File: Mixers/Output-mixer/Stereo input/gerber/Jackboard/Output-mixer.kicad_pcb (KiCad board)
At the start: 2 copper layers, 135 x 110 mm, 131 parts, among them J1 In, J10 In, J11 In, J12 In, J14 Conn_01x04_Female, J17 Conn_01x02_Female, J2 In, J21 Jack 3.5 Out, J22 OutL, J23 OutR, J25 Conn_01x02_Female, J3 In, J4 In, J5 In, J6 In, J7 In, J8 In, J9 In, Q10 2N3904, Q5 2N3904, Q6 2N3904, Q7 2N3904, Q8 2N3904, Q9 2N3904, SW1 Mute, SW2 Mute, SW3 Mute, SW4 Mute, SW5 Mute, SW6 Mute, U1 TL072, U2 TL072, U3 TL072

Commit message: update gerbers for stereo mixer
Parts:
- removed C1, C2, C3, C4, C5, C6: .1µF, Capacitor_THT:CP_Radial_D5.0mm_P2.00mm
- removed C11, C14, C15, C16, C17, C18: 100nF, Capacitor_THT:C_Disc_D7.0mm_W2.5mm_P5.00mm
- removed the D1 at (76.4, 86.5)
- removed the D2 at (76.4, 105.0)
- removed the D3 at (76.4, 142.0)
- removed the D4 at (76.4, 49.5)
- removed the D5 at (76.4, 68.0)
- removed the D6 at (76.4, 123.5)
- removed Gain1, Gain2, Gain3, Gain4, Gain5, Gain6: 500k, Synth:Pot-bourns-alpha
- removed R1, R2, R3, R4, R5, R6: 2.2k, Resistor_THT:R_Axial_DIN0207_L6.3mm_D2.5mm_P10.16mm_Horizontal
- removed R10, R11, R12, R7, R8, R9: 100k, Resistor_THT:R_Axial_DIN0207_L6.3mm_D2.5mm_P10.16mm_Horizontal
- removed the R13 at (106.5, 41.8)
- removed the R14 at (107.0, 65.8)
- removed the R15 at (106.9, 76.0)
- removed the R16 at (107.3, 103.3)
- removed the R17 at (107.3, 113.0)
- removed the R18 at (107.5, 134.8)
- removed U1, U2, U3: TL072, Package_DIP:DIP-8_W7.62mm_Socket
- added J27: Conn_01x06_Female, Connector_PinSocket_2.54mm:PinSocket_1x06_P2.54mm_Vertical, B.Cu at (52.8, 45.8)
- added J28: Conn_01x06_Female, Connector_PinSocket_2.54mm:PinSocket_1x06_P2.54mm_Vertical, B.Cu at (52.8, 64.2)
- added J29: Conn_01x06_Female, Connector_PinSocket_2.54mm:PinSocket_1x06_P2.54mm_Vertical, B.Cu at (52.8, 82.8)
- added J30: Conn_01x06_Female, Connector_PinSocket_2.54mm:PinSocket_1x06_P2.54mm_Vertical, B.Cu at (52.8, 101.2)
- added J35: Conn_01x06_Female, Connector_PinSocket_2.54mm:PinSocket_1x06_P2.54mm_Vertical, B.Cu at (52.8, 119.8)
- added J36: Conn_01x06_Female, Connector_PinSocket_2.54mm:PinSocket_1x06_P2.54mm_Vertical, B.Cu at (52.8, 138.2)
- added J40: Conn_01x04_Female, Connector_PinSocket_2.54mm:PinSocket_1x04_P2.54mm_Vertical, B.Cu at (82.2, 81.8)
- added RV1: 50k, Synth:PTV1124420AA503, F.Cu at (72.8, 42.5)
- added RV2: 50k, Synth:PTV1124420AA503, F.Cu at (72.8, 61.0)
- added RV3: 50k, Synth:PTV1124420AA503, F.Cu at (72.8, 79.5)
- added RV4: 50k, Synth:PTV1124420AA503, F.Cu at (72.8, 98.0)
- added RV5: 50k, Synth:PTV1124420AA503, F.Cu at (72.8, 116.5)
- added RV6: 50k, Synth:PTV1124420AA503, F.Cu at (72.8, 135.0)
- moved J10 41.6 mm to (22.0, 107.0)
- moved J12 41.6 mm to (22.0, 125.5)
- moved J6 41.6 mm to (22.0, 70.0)
- moved R21 40.7 mm to (82.0, 139.1), turned to 90 degrees
- moved R14 35.0 mm to (85.5, 54.2), turned to -90 degrees
- moved R22 33.5 mm to (85.5, 128.9), turned to -90 degrees
- moved R20 33.2 mm to (85.5, 110.6), turned to -90 degrees
- moved R18 32.6 mm to (86.1, 97.5)
- moved R15 32.4 mm to (76.0, 73.0)
- moved R24 32.3 mm to (85.5, 36.5), turned to -90 degrees
- moved Pan1 31.8 mm to (97.0, 65.5)
- moved Pan2 31.8 mm to (97.0, 84.0)
- moved Pan3 31.8 mm to (97.0, 102.5)
- moved Pan4 31.8 mm to (97.0, 121.0)
- moved Pan5 31.8 mm to (97.0, 139.6)
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- renumbered D7 to D1, D8 to D2, D9 to D3, D10 to D4, D11 to D5, D12 to D6, Pan2 to Pan1, Pan3 to Pan2, Pan4 to Pan3, Pan5 to Pan4, Pan6 to Pan5, Pan1 to Pan6, R21 to R13, R22 to R14, R23 to R15, R24 to R16, R25 to R17, R26 to R18, R27 to R19, R28 to R20, R29 to R21, R30 to R22, R19 to R23, R20 to R24, R31 to R25, R32 to R26, R33 to R27, R34 to R28, R35 to R29, R36 to R30, R37 to R31, R38 to R32, R39 to R33, R40 to R34, R41 to R35, R42 to R36, R59 to R53, R60 to R54, R61 to R55, R62 to R56, R63 to R57, R64 to R58, R65 to R59, R66 to R60, R67 to R61, R68 to R62, R69 to R63, R70 to R64, RV1 to RV7, RV2 to RV8, SW2 to SW1, SW4 to SW2, SW1 to SW3, SW3 to SW4, SW6 to SW5, SW5 to SW6
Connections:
- J1 pad TN: unconnected-(J1-PadTN) -> Net-(J1-PadTN)
- J10 pad TN: unconnected-(J10-PadTN) -> Net-(J10-PadTN)
- J11 pad TN: unconnected-(J11-PadTN) -> Net-(J11-PadTN)
- J12 pad T: Net-(J11-PadT) -> Net-(J11-PadTN)
- J12 pad TN: unconnected-(J12-PadTN) -> Net-(J11-PadT)
- J2 pad T: Net-(J1-PadT) -> Net-(J1-PadTN)
- J2 pad TN: unconnected-(J2-PadTN) -> Net-(J1-PadT)
- J3 pad TN: unconnected-(J3-PadTN) -> Net-(J3-PadTN)
- J4 pad T: Net-(J3-PadT) -> Net-(J3-PadTN)
- J4 pad TN: unconnected-(J4-PadTN) -> Net-(J3-PadT)
- J5 pad TN: unconnected-(J5-PadTN) -> Net-(J5-PadTN)
- J6 pad T: Net-(J5-PadT) -> Net-(J5-PadTN)
- J6 pad TN: unconnected-(J6-PadTN) -> Net-(J5-PadT)
- J7 pad TN: unconnected-(J7-PadTN) -> Net-(J7-PadTN)
- J8 pad T: Net-(J7-PadT) -> Net-(J7-PadTN)
- J8 pad TN: unconnected-(J8-PadTN) -> Net-(J7-PadT)
- J9 pad T: Net-(J10-PadT) -> Net-(J10-PadTN)
- J9 pad TN: unconnected-(J9-PadTN) -> Net-(J10-PadT)
- R13 pad 1: Net-(Gain2-Pad1) -> Right2_Out
- R14 pad 2: Net-(Gain2-Pad1) -> Left2_Out
- R15 pad 1: Net-(Gain3-Pad1) -> Right3_Out
- R16 pad 2: Net-(Gain3-Pad1) -> Left3_Out
- R17 pad 1: Net-(Gain4-Pad1) -> Right4_Out
- R18 pad 2: Net-(Gain4-Pad1) -> Left4_Out
- R19 pad 1: Net-(Gain5-Pad1) -> Right5_Out
- R20 pad 2: Net-(Gain5-Pad1) -> Left5_Out
- R21 pad 1: Net-(Gain6-Pad1) -> Right6_Out
- R22 pad 2: Net-(Gain6-Pad1) -> Left6_Out
- R23 pad 1: Net-(Gain1-Pad1) -> Right1_Out
- R24 pad 2: Net-(Gain1-Pad1) -> Left1_Out
- R53 pad 1: In3 -> Right3_In
- R55 pad 1: In4 -> Right4_In
- R57 pad 1: In1 -> Right1_In
- R58 pad 1: In5 -> Right5_In
- R61 pad 1: In6 -> Right6_In
- R62 pad 1: In2 -> Right2_In
- SW1 pad 1: GND -> Right6_In
- SW1 pad 2: Net-(D3-Pad1) -> Net-(J11-PadT)
- SW1 pad 4: unconnected-(SW2-Pad4) -> Left6_In
- SW1 pad 5: Net-(J11-PadT) -> Net-(J11-PadTN)
- SW1 pad 6: In6 -> unconnected-(SW1-Pad6)
- SW2 pad 1: GND -> Right1_In
- SW2 pad 2: Net-(D4-Pad1) -> Net-(J1-PadT)
- SW2 pad 4: unconnected-(SW4-Pad4) -> Left1_In
- SW2 pad 5: Net-(J1-PadT) -> Net-(J1-PadTN)
- SW2 pad 6: In1 -> unconnected-(SW2-Pad6)
- SW3 pad 1: GND -> Right3_In
- SW3 pad 2: Net-(D1-Pad1) -> Net-(J5-PadT)
- SW3 pad 4: unconnected-(SW1-Pad4) -> Left3_In
- SW3 pad 5: Net-(J5-PadT) -> Net-(J5-PadTN)
- SW3 pad 6: In3 -> unconnected-(SW3-Pad6)
- SW4 pad 1: GND -> Right2_In
- SW4 pad 2: Net-(D5-Pad1) -> Net-(J3-PadT)
- SW4 pad 4: unconnected-(SW3-Pad4) -> Left2_In
- SW4 pad 5: Net-(J3-PadT) -> Net-(J3-PadTN)
- SW4 pad 6: In2 -> unconnected-(SW4-Pad6)
- SW5 pad 1: GND -> Right4_In
- SW5 pad 2: Net-(D2-Pad1) -> Net-(J7-PadT)
- SW5 pad 4: unconnected-(SW6-Pad4) -> Left4_In
- SW5 pad 5: Net-(J7-PadT) -> Net-(J7-PadTN)
- SW5 pad 6: In4 -> unconnected-(SW5-Pad6)
- SW6 pad 1: GND -> Right5_In
- SW6 pad 2: Net-(D6-Pad1) -> Net-(J10-PadTN)
- SW6 pad 4: unconnected-(SW5-Pad4) -> Left5_In
- SW6 pad 6: In5 -> unconnected-(SW6-Pad6)
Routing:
- net +12V: track 376.0 -> 194.5 mm
- net -12V: track 191.0 -> 76.3 mm
- net Right4_In: track 0.00 -> 70.0 mm
- net Right5_In: track 0.00 -> 68.8 mm
- net Right3_In: track 0.00 -> 68.8 mm
- net Right2_In: track 0.00 -> 68.8 mm
- net Right6_In: track 0.00 -> 68.8 mm
- net Right1_In: track 0.00 -> 67.3 mm
- net In6: track 67.0 -> 0.00 mm
- net In3: track 62.9 -> 0.00 mm
- net In5: track 62.6 -> 0.00 mm
- net In1: track 62.6 -> 0.00 mm
- net In4: track 61.4 -> 0.00 mm
- net In2: track 61.3 -> 0.00 mm
- net Net-(Gain6-Pad1): track 46.7 -> 0.00 mm
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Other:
- board text added: "Board 1/3"

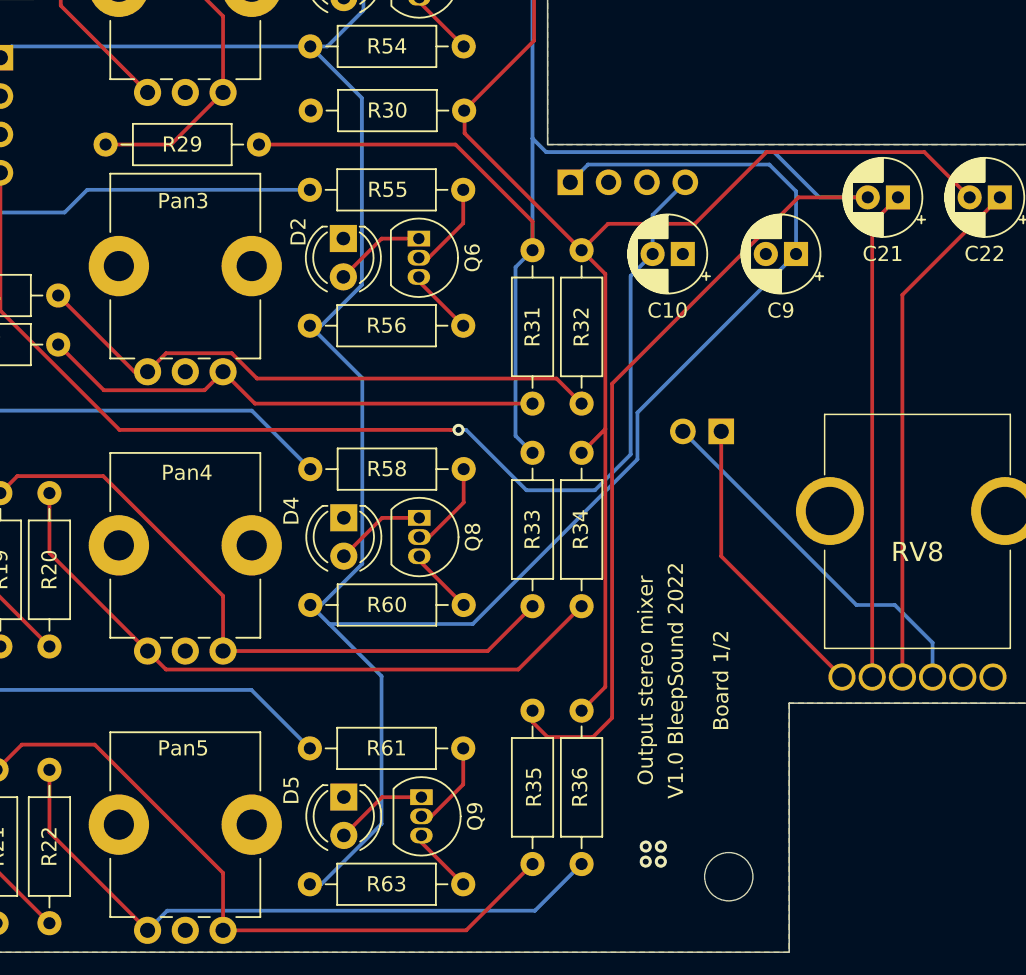
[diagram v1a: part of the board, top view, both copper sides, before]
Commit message: update gerber for DC mixer and update jackboard on output mixer
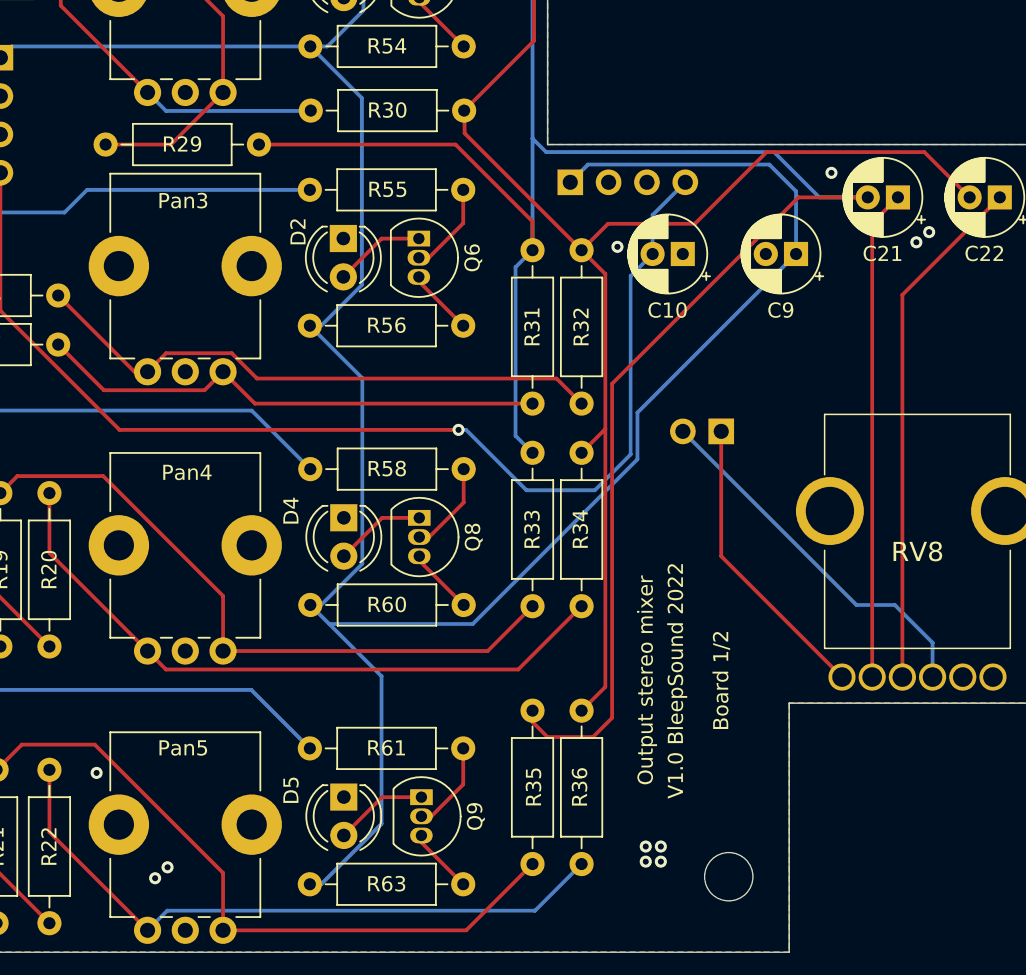
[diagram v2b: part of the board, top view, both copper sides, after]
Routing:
- net Net-(Pan2-Pad3): track 9.93 -> 21.3 mm
- net GND: vias 4 -> 11
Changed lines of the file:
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@@
     )
     (fp_line (start 6.6 6.35) (end 6.6 3.35) (layer "F.SilkS") (width 0.12))
+    (fp_line (start -6.6 3.35) (end -6.6 -6.35) (layer "F.SilkS") (width 0.12))
     (fp_line (start -6.4 -6.35) (end -6.6 -6.35) (layer "F.SilkS") (width 0.12))
     (fp_line (start 3 0) (end 1.2 -2.75) (layer "F.SilkS") (width 0.12))
@@
     (fp_line (start 6.6 6.35) (end -6.6 6.35) (layer "F.SilkS") (width 0.12))
     (fp_line (start -6.6 6.35) (end -6.6 3.35) (layer "F.SilkS") (width 0.12))
+    (fp_line (start 0 -6.35) (end 6.6 -6.35) (layer "F.SilkS") (width 0.12))
     (fp_line (start -1.2 2.75) (end -3 0) (layer "F.SilkS") (width 0.12))
-    (fp_line (start 0 -6.35) (end 6.6 -6.35) (layer "F.SilkS") (width 0.12))
     (fp_line (start -6 -6.35) (end -6.4 -6.35) (layer "F.SilkS") (width 0.12))
     (fp_line (start 3 0) (end 1.2 2.75) (layer "F.SilkS") (width 0.12))
+    (fp_line (start 0 -6.35) (end -6 -6.35) (layer "F.SilkS") (width 0.12))
     (fp_line (start -1.2 -2.75) (end 1.2 -2.75) (layer "F.SilkS") (width 0.12))
     (fp_line (start -1.2 2.75) (end 1.2 2.75) (layer "F.SilkS") (width 0.12))
-    (fp_line (start 0 -6.35) (end -6 -6.35) (layer "F.SilkS") (width 0.12))
-    (fp_line (start -6.6 3.35) (end -6.6 -6.35) (layer "F.SilkS") (width 0.12))
     (fp_line (start -3 0) (end -1.2 -2.75) (layer "F.SilkS") (width 0.12))
     (fp_circle (center 0 0) (end 3 0) (layer "F.SilkS") (width 0.12) (fill none))
@@
   (segment (start 86.25 78.3) (end 92 84.05) (width 0.25) (layer "F.Cu") (net 27))
   (segment (start 86.25 76.5) (end 86.25 78.3) (width 0.25) (layer "F.Cu") (net 27))
+  (segment (start 93.224511 85.274511) (end 102.785489 85.274511) (width 0.25) (layer "B.Cu") (net 27))
+  (segment (start 102.785489 85.274511) (end 102.81 85.25) (width 0.25) (layer "B.Cu") (net 27))
+  (segment (start 92 84.05) (end 93.224511 85.274511) (width 0.25) (layer "B.Cu") (net 27))
   (segment (start 86.08 100.75) (end 89.104511 103.774511) (width 0.25) (layer "F.Cu") (net 28))
   (segment (start 117.5 104.66) (end 99.11 104.66) (width 0.25) (layer "F.Cu") (net 28))
@@
   (segment (start 55.46 133) (end 52.75 135.71) (width 0.25) (layer "B.Cu") (net 94))
   (segment (start 72.775 133) (end 55.46 133) (width 0.25) (layer "B.Cu") (net 94))
+  (via (at 92.5 136.1) (size 0.8) (drill 0.4) (layers "F.Cu" "B.Cu") (free) (net 96))
+  (via (at 88.625 129.125) (size 0.8) (drill 0.4) (layers "F.Cu" "B.Cu") (free) (net 96))
+  (via (at 123.125 94.275) (size 0.8) (drill 0.4) (layers "F.Cu" "B.Cu") (free) (net 96))
+  (via (at 93.325 135.375) (size 0.8) (drill 0.4) (layers "F.Cu" "B.Cu") (free) (net 96))
   (via (at 126 135) (size 0.8) (drill 0.4) (layers "F.Cu" "B.Cu") (free) (net 96))
   (via (at 125 135) (size 0.8) (drill 0.4) (layers "F.Cu" "B.Cu") (free) (net 96))
   (via (at 126 134) (size 0.8) (drill 0.4) (layers "F.Cu" "B.Cu") (free) (net 96))
+  (via (at 143.775 93.3) (size 0.8) (drill 0.4) (layers "F.Cu" "B.Cu") (free) (net 96))
+  (via (at 142.925 93.975) (size 0.8) (drill 0.4) (layers "F.Cu" "B.Cu") (free) (net 96))
+  (via (at 137.3 89.375) (size 0.8) (drill 0.4) (layers "F.Cu" "B.Cu") (free) (net 96))
   (via (at 125 134) (size 0.8) (drill 0.4) (layers "F.Cu" "B.Cu") (free) (net 96))
   (segment (start 112.91 92.714022) (end 112.91 90.5) (width 0.25) (layer "F.Cu") (net 97))
